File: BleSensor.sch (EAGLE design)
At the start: 13 parts, among them T1 BPW85C, U1 PIC12F1572/P

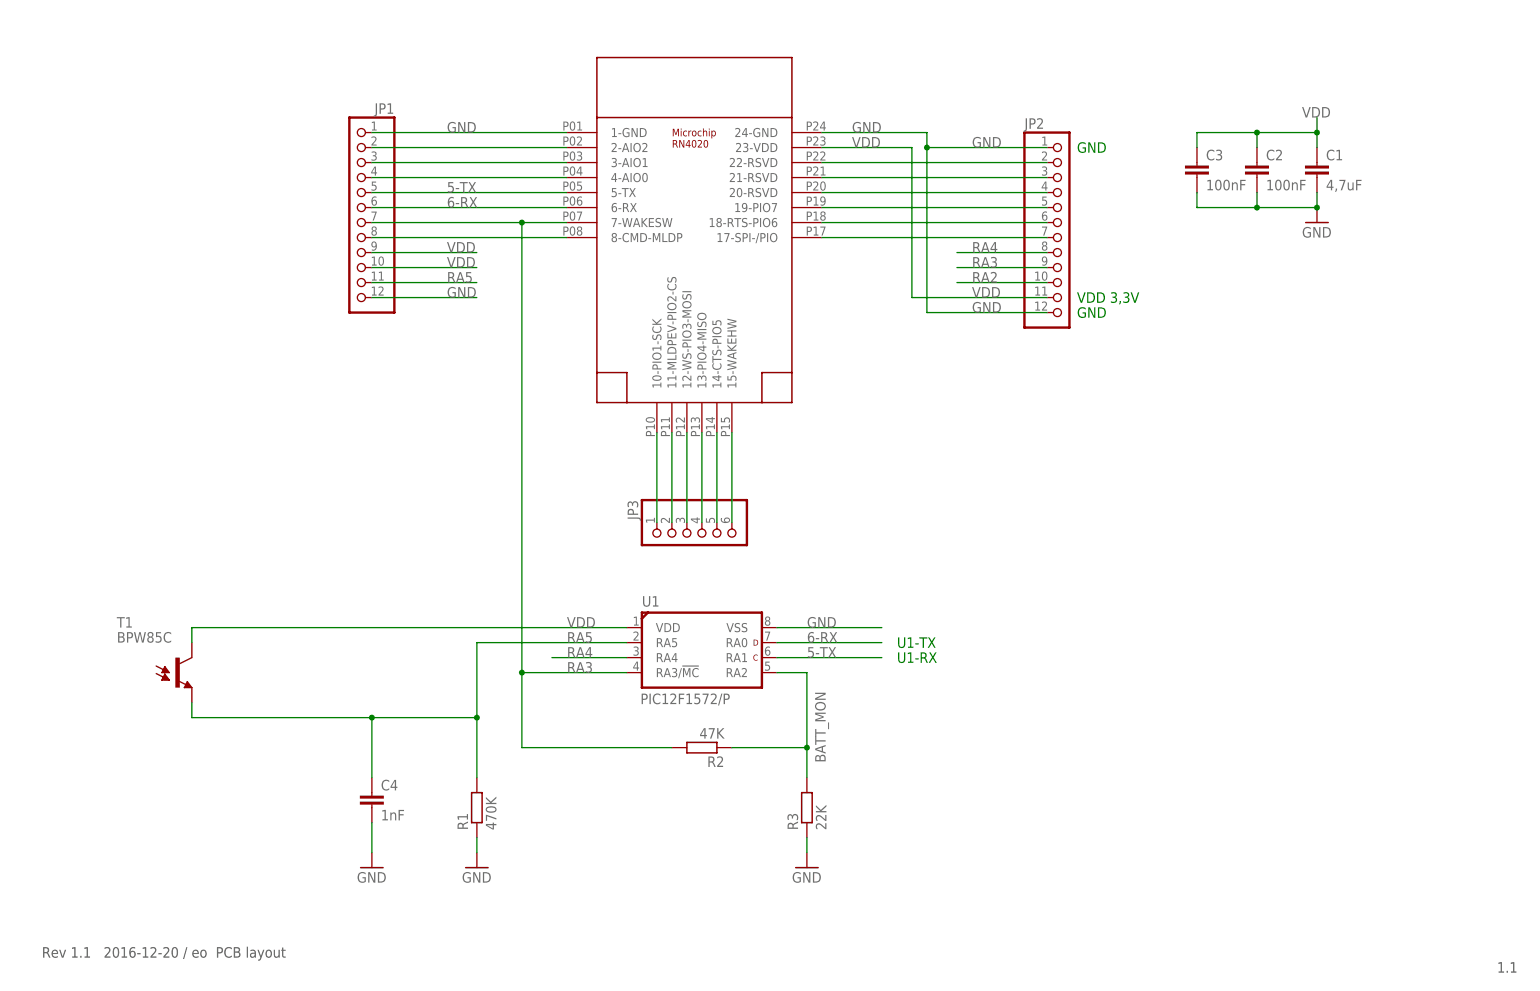
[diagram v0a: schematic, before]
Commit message: Added sensors
Added sensors
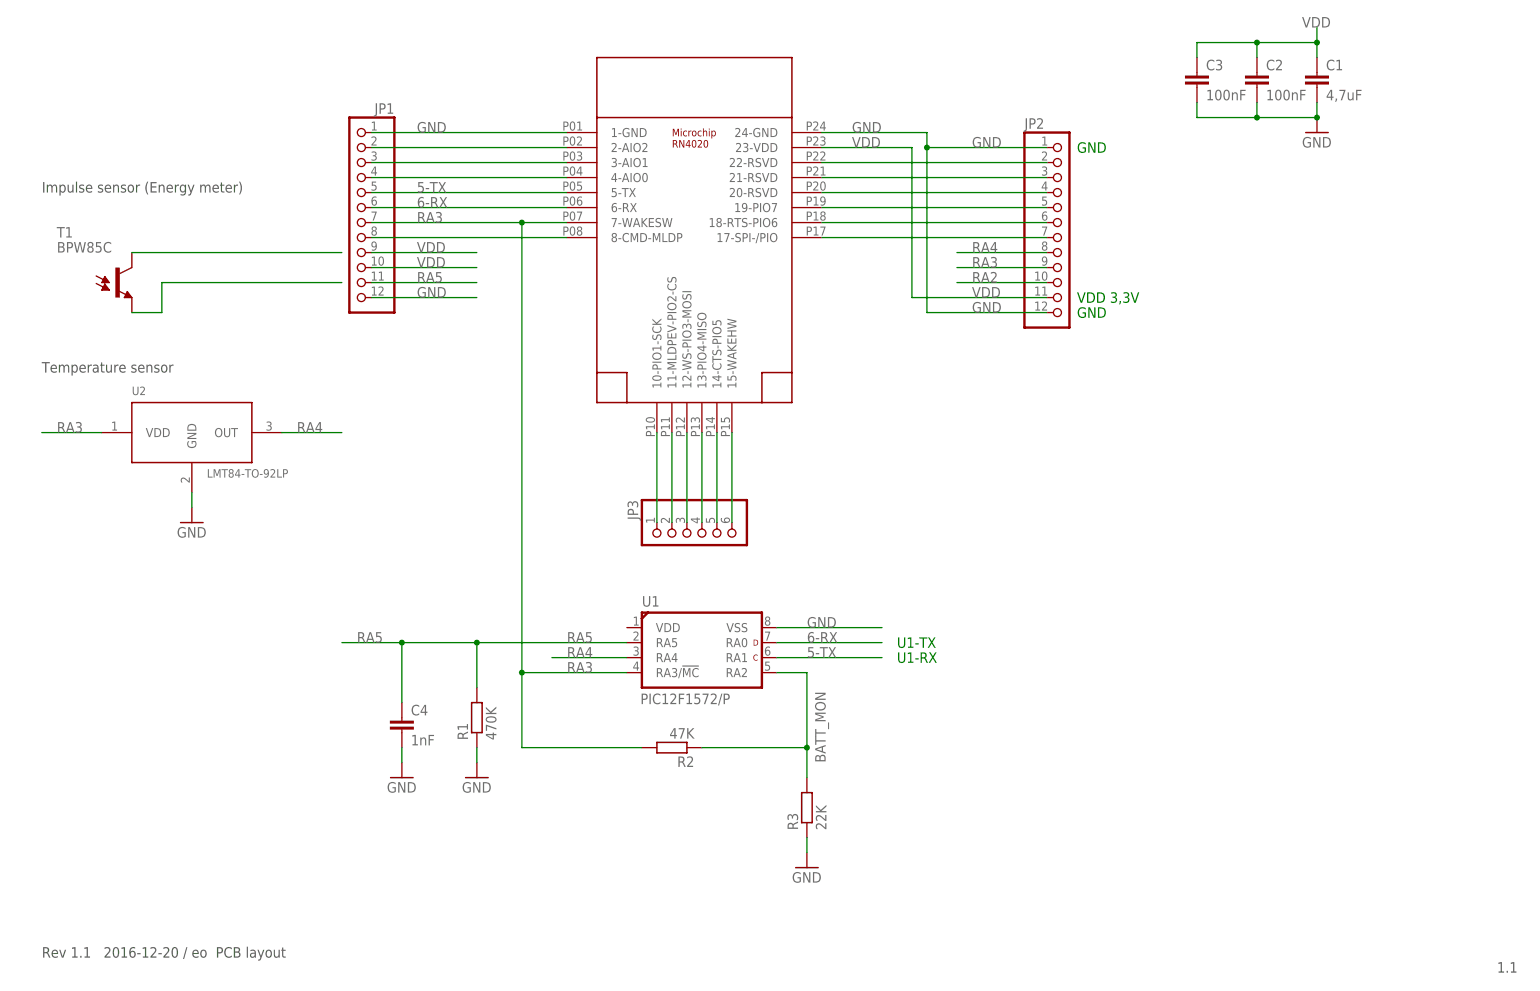
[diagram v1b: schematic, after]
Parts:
- added U2: LMT84-TO-92LP, Temperature sensor:LMT84-TO-92LP
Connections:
- new net N$13: T1.E
- net GND: now also U2.GND
- net RA3: now also U2.VDD
- net RA4: now also U2.OUT
- net RA5: no longer T1.E
- net VDD: no longer T1.C, U1.VDD
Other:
- note added: "Impulse sensor (Energy meter)"
- note added: "Temperature sensor"
- moved on the sheet: C1, C2, C3, C4, R1, R2, T1

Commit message: Fixed sensor inputs, added pdf Bitscope BLE Sensor pics
Fixed sensor inputs, added pdf Bitscope BLE Sensor pics
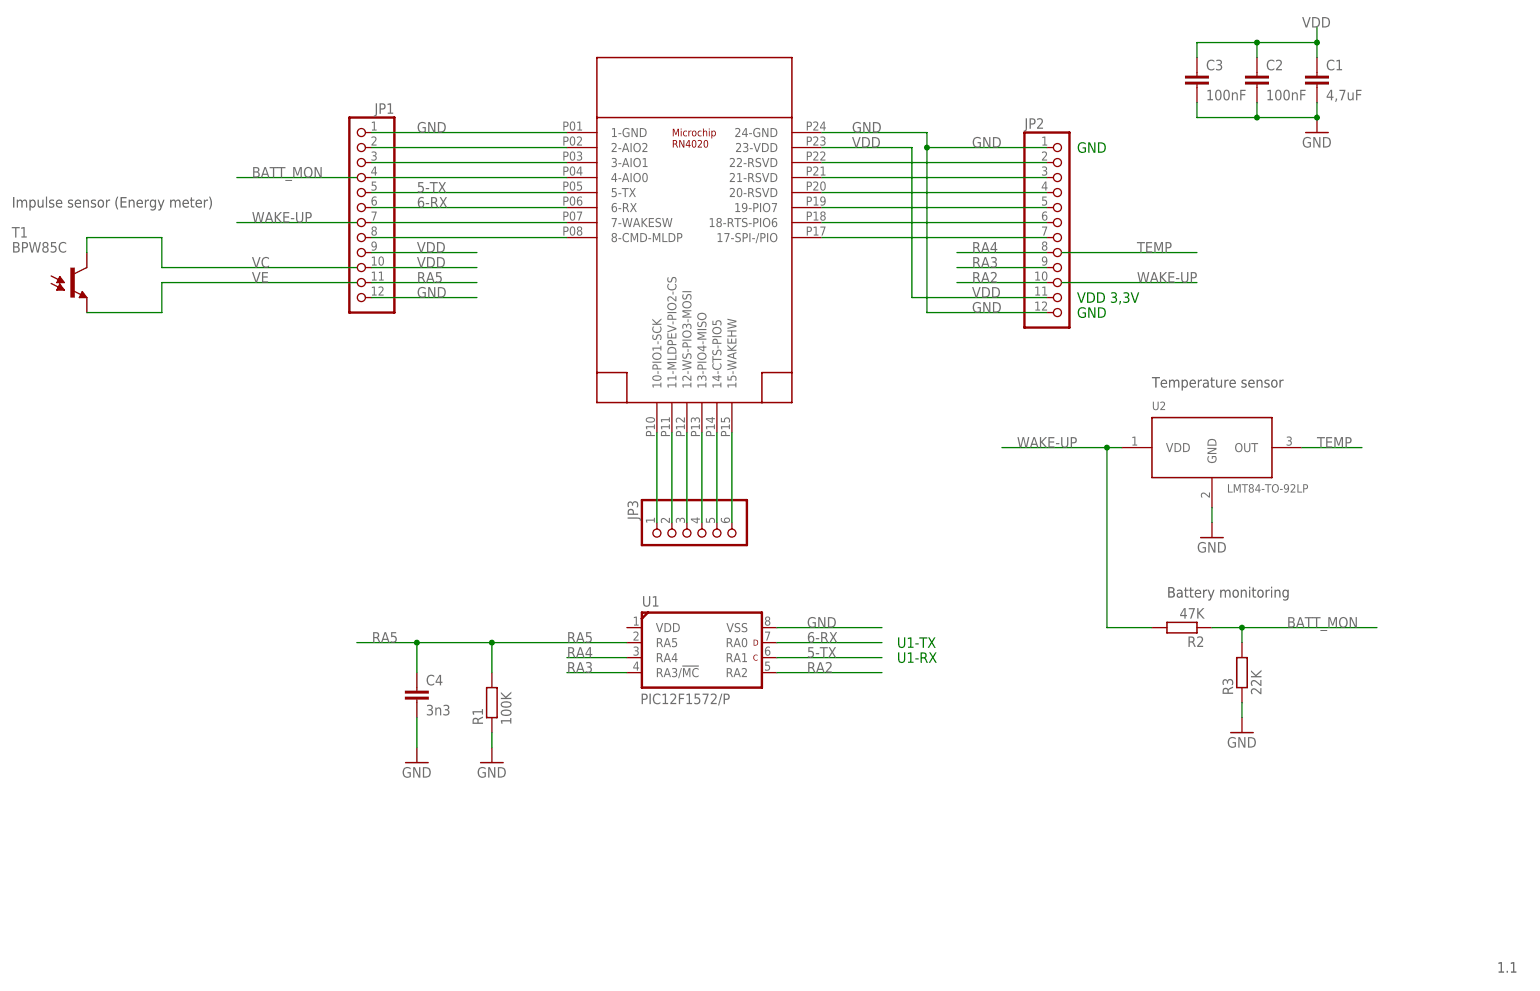
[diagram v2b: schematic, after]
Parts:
- C4: value 1nF -> 3n3
- R1: value 470K -> 100K
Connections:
- net N$13 renamed VE
- removed net N$12: JP1.4, U$1.4-AIO0
- new net TEMP: U2.OUT
- new net VC: T1.C
- new net WAKE-UP: R2.2, U2.VDD
- net BATT_MON: now also JP1.4, U$1.4-AIO0; no longer U1.RA2
- net RA2: now also JP1.7, U$1.7-WAKESW, U1.RA2
- net RA3: no longer JP1.7, R2.2, U$1.7-WAKESW, U2.VDD
- net RA4: no longer U2.OUT
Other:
- note added: "Battery monitoring"
- note removed: "Rev 1.1 2016-12-20 / eo PCB layout"
- moved on the sheet: C4, R1, R2, R3, T1, U2
